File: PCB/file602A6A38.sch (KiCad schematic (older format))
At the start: 27 parts, among them IC4 74LV1T125GVH, IC5 74LV1T125GVH

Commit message: Completed parts details on schematics and recreated gerbers and bom.
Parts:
- IC4, IC5: LCSC (none) -> C75925
- R11, R12, R13, R14, R27, R28, R29, R31, R32, R33, R34, R35, R36, R37, R38, R39, R40, R41, R42, R43: LCSC (none) -> C17414; Manufacturer_Name (none) -> Vishay; Manufacturer_Part_Number (none) -> CRCW080510K0FKEAC; Mouser Part Number (none) -> 71-CRCW080510K0FKEAC
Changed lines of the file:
@@
 F 8 "Nexperia" H 3700 1700 50  0001 L CNN "Manufacturer_Name"
 F 9 "74LV1T125GVH" H 3700 1600 50  0001 L CNN "Manufacturer_Part_Number"
+F 10 "C75925" H 2850 2200 50  0001 C CNN "LCSC"
 	1    2850 2200
 	-1   0    0    1
@@
 F 8 "Nexperia" H 3700 2400 50  0001 L CNN "Manufacturer_Name"
 F 9 "74LV1T125GVH" H 3700 2300 50  0001 L CNN "Manufacturer_Part_Number"
+F 10 "C75925" H 2850 2900 50  0001 C CNN "LCSC"
 	1    2850 2900
 	-1   0    0    1
@@
 F 2 "Resistor_SMD:R_0805_2012Metric_Pad1.15x1.40mm_HandSolder" H 6600 2150 50  0001 C CNN
 F 3 "~" H 6600 2150 50  0001 C CNN
+F 4 "C17414" H 6600 2150 50  0001 C CNN "LCSC"
+F 5 "Vishay" H 6600 2150 50  0001 C CNN "Manufacturer_Name"
+F 6 "CRCW080510K0FKEAC" H 6600 2150 50  0001 C CNN "Manufacturer_Part_Number"
+F 7 "71-CRCW080510K0FKEAC" H 6600 2150 50  0001 C CNN "Mouser Part Number"
 	1    6600 2150
 	-1   0    0    1
@@
 F 2 "Resistor_SMD:R_0805_2012Metric_Pad1.15x1.40mm_HandSolder" H 6600 1250 50  0001 C CNN
 F 3 "~" H 6600 1250 50  0001 C CNN
+F 4 "C17414" H 6600 1250 50  0001 C CNN "LCSC"
+F 5 "Vishay" H 6600 1250 50  0001 C CNN "Manufacturer_Name"
+F 6 "CRCW080510K0FKEAC" H 6600 1250 50  0001 C CNN "Manufacturer_Part_Number"
+F 7 "71-CRCW080510K0FKEAC" H 6600 1250 50  0001 C CNN "Mouser Part Number"
 	1    6600 1250
 	1    0    0    -1
@@
 F 2 "Resistor_SMD:R_0805_2012Metric_Pad1.15x1.40mm_HandSolder" H 6500 1150 50  0001 C CNN
 F 3 "~" H 6500 1150 50  0001 C CNN
+F 4 "C17414" H 6500 1150 50  0001 C CNN "LCSC"
+F 5 "Vishay" H 6500 1150 50  0001 C CNN "Manufacturer_Name"
+F 6 "CRCW080510K0FKEAC" H 6500 1150 50  0001 C CNN "Manufacturer_Part_Number"
+F 7 "71-CRCW080510K0FKEAC" H 6500 1150 50  0001 C CNN "Mouser Part Number"
 	1    6500 1150
 	1    0    0    -1
@@
 F 2 "Resistor_SMD:R_0805_2012Metric_Pad1.15x1.40mm_HandSolder" H 6500 2050 50  0001 C CNN
 F 3 "~" H 6500 2050 50  0001 C CNN
+F 4 "C17414" H 6500 2050 50  0001 C CNN "LCSC"
+F 5 "Vishay" H 6500 2050 50  0001 C CNN "Manufacturer_Name"
+F 6 "CRCW080510K0FKEAC" H 6500 2050 50  0001 C CNN "Manufacturer_Part_Number"
+F 7 "71-CRCW080510K0FKEAC" H 6500 2050 50  0001 C CNN "Mouser Part Number"
 	1    6500 2050
 	-1   0    0    1
@@
 F 2 "Resistor_SMD:R_0805_2012Metric_Pad1.15x1.40mm_HandSolder" H 9050 2200 50  0001 C CNN
 F 3 "~" H 9050 2200 50  0001 C CNN
+F 4 "C17414" H 9050 2200 50  0001 C CNN "LCSC"
+F 5 "Vishay" H 9050 2200 50  0001 C CNN "Manufacturer_Name"
+F 6 "CRCW080510K0FKEAC" H 9050 2200 50  0001 C CNN "Manufacturer_Part_Number"
+F 7 "71-CRCW080510K0FKEAC" H 9050 2200 50  0001 C CNN "Mouser Part Number"
 	1    9050 2200
 	-1   0    0    1
@@
 F 2 "Resistor_SMD:R_0805_2012Metric_Pad1.15x1.40mm_HandSolder" H 9050 1300 50  0001 C CNN
 F 3 "~" H 9050 1300 50  0001 C CNN
+F 4 "C17414" H 9050 1300 50  0001 C CNN "LCSC"
+F 5 "Vishay" H 9050 1300 50  0001 C CNN "Manufacturer_Name"
+F 6 "CRCW080510K0FKEAC" H 9050 1300 50  0001 C CNN "Manufacturer_Part_Number"
+F 7 "71-CRCW080510K0FKEAC" H 9050 1300 50  0001 C CNN "Mouser Part Number"
 	1    9050 1300
 	1    0    0    -1
@@
 F 2 "Resistor_SMD:R_0805_2012Metric_Pad1.15x1.40mm_HandSolder" H 8950 1200 50  0001 C CNN
 F 3 "~" H 8950 1200 50  0001 C CNN
+F 4 "C17414" H 8950 1200 50  0001 C CNN "LCSC"
+F 5 "Vishay" H 8950 1200 50  0001 C CNN "Manufacturer_Name"
+F 6 "CRCW080510K0FKEAC" H 8950 1200 50  0001 C CNN "Manufacturer_Part_Number"
+F 7 "71-CRCW080510K0FKEAC" H 8950 1200 50  0001 C CNN "Mouser Part Number"
 	1    8950 1200
 	1    0    0    -1
@@
 F 2 "Resistor_SMD:R_0805_2012Metric_Pad1.15x1.40mm_HandSolder" H 8950 2100 50  0001 C CNN
 F 3 "~" H 8950 2100 50  0001 C CNN
+F 4 "C17414" H 8950 2100 50  0001 C CNN "LCSC"
+F 5 "Vishay" H 8950 2100 50  0001 C CNN "Manufacturer_Name"
+F 6 "CRCW080510K0FKEAC" H 8950 2100 50  0001 C CNN "Manufacturer_Part_Number"
+F 7 "71-CRCW080510K0FKEAC" H 8950 2100 50  0001 C CNN "Mouser Part Number"
 	1    8950 2100
 	-1   0    0    1
@@
 F 2 "Resistor_SMD:R_0805_2012Metric_Pad1.15x1.40mm_HandSolder" H 6550 4350 50  0001 C CNN
 F 3 "~" H 6550 4350 50  0001 C CNN
+F 4 "C17414" H 6550 4350 50  0001 C CNN "LCSC"
+F 5 "Vishay" H 6550 4350 50  0001 C CNN "Manufacturer_Name"
+F 6 "CRCW080510K0FKEAC" H 6550 4350 50  0001 C CNN "Manufacturer_Part_Number"
+F 7 "71-CRCW080510K0FKEAC" H 6550 4350 50  0001 C CNN "Mouser Part Number"
 	1    6550 4350
 	-1   0    0    1
@@
 F 2 "Resistor_SMD:R_0805_2012Metric_Pad1.15x1.40mm_HandSolder" H 6550 3450 50  0001 C CNN
 F 3 "~" H 6550 3450 50  0001 C CNN
+F 4 "C17414" H 6550 3450 50  0001 C CNN "LCSC"
+F 5 "Vishay" H 6550 3450 50  0001 C CNN "Manufacturer_Name"
+F 6 "CRCW080510K0FKEAC" H 6550 3450 50  0001 C CNN "Manufacturer_Part_Number"
+F 7 "71-CRCW080510K0FKEAC" H 6550 3450 50  0001 C CNN "Mouser Part Number"
 	1    6550 3450
 	1    0    0    -1
@@
 F 2 "Resistor_SMD:R_0805_2012Metric_Pad1.15x1.40mm_HandSolder" H 6450 3350 50  0001 C CNN
 F 3 "~" H 6450 3350 50  0001 C CNN
+F 4 "C17414" H 6450 3350 50  0001 C CNN "LCSC"
+F 5 "Vishay" H 6450 3350 50  0001 C CNN "Manufacturer_Name"
+F 6 "CRCW080510K0FKEAC" H 6450 3350 50  0001 C CNN "Manufacturer_Part_Number"
+F 7 "71-CRCW080510K0FKEAC" H 6450 3350 50  0001 C CNN "Mouser Part Number"
 	1    6450 3350
 	1    0    0    -1
@@
 F 2 "Resistor_SMD:R_0805_2012Metric_Pad1.15x1.40mm_HandSolder" H 6450 4250 50  0001 C CNN
 F 3 "~" H 6450 4250 50  0001 C CNN
+F 4 "C17414" H 6450 4250 50  0001 C CNN "LCSC"
+F 5 "Vishay" H 6450 4250 50  0001 C CNN "Manufacturer_Name"
+F 6 "CRCW080510K0FKEAC" H 6450 4250 50  0001 C CNN "Manufacturer_Part_Number"
+F 7 "71-CRCW080510K0FKEAC" H 6450 4250 50  0001 C CNN "Mouser Part Number"
 	1    6450 4250
 	-1   0    0    1
@@
 F 2 "Resistor_SMD:R_0805_2012Metric_Pad1.15x1.40mm_HandSolder" H 9050 4350 50  0001 C CNN
 F 3 "~" H 9050 4350 50  0001 C CNN
+F 4 "C17414" H 9050 4350 50  0001 C CNN "LCSC"
+F 5 "Vishay" H 9050 4350 50  0001 C CNN "Manufacturer_Name"
+F 6 "CRCW080510K0FKEAC" H 9050 4350 50  0001 C CNN "Manufacturer_Part_Number"
+F 7 "71-CRCW080510K0FKEAC" H 9050 4350 50  0001 C CNN "Mouser Part Number"
 	1    9050 4350
 	-1   0    0    1
@@
 F 2 "Resistor_SMD:R_0805_2012Metric_Pad1.15x1.40mm_HandSolder" H 9050 3450 50  0001 C CNN
 F 3 "~" H 9050 3450 50  0001 C CNN
+F 4 "C17414" H 9050 3450 50  0001 C CNN "LCSC"
+F 5 "Vishay" H 9050 3450 50  0001 C CNN "Manufacturer_Name"
+F 6 "CRCW080510K0FKEAC" H 9050 3450 50  0001 C CNN "Manufacturer_Part_Number"
+F 7 "71-CRCW080510K0FKEAC" H 9050 3450 50  0001 C CNN "Mouser Part Number"
 	1    9050 3450
 	1    0    0    -1
@@
 F 2 "Resistor_SMD:R_0805_2012Metric_Pad1.15x1.40mm_HandSolder" H 8950 3350 50  0001 C CNN
 F 3 "~" H 8950 3350 50  0001 C CNN
+F 4 "C17414" H 8950 3350 50  0001 C CNN "LCSC"
+F 5 "Vishay" H 8950 3350 50  0001 C CNN "Manufacturer_Name"
+F 6 "CRCW080510K0FKEAC" H 8950 3350 50  0001 C CNN "Manufacturer_Part_Number"
+F 7 "71-CRCW080510K0FKEAC" H 8950 3350 50  0001 C CNN "Mouser Part Number"
 	1    8950 3350
 	1    0    0    -1
@@
 F 2 "Resistor_SMD:R_0805_2012Metric_Pad1.15x1.40mm_HandSolder" H 8950 4250 50  0001 C CNN
 F 3 "~" H 8950 4250 50  0001 C CNN
+F 4 "C17414" H 8950 4250 50  0001 C CNN "LCSC"
+F 5 "Vishay" H 8950 4250 50  0001 C CNN "Manufacturer_Name"
+F 6 "CRCW080510K0FKEAC" H 8950 4250 50  0001 C CNN "Manufacturer_Part_Number"
+F 7 "71-CRCW080510K0FKEAC" H 8950 4250 50  0001 C CNN "Mouser Part Number"
 	1    8950 4250
 	-1   0    0    1
@@
 F 2 "Resistor_SMD:R_0805_2012Metric_Pad1.15x1.40mm_HandSolder" H 7750 1200 50  0001 C CNN
 F 3 "~" H 7750 1200 50  0001 C CNN
+F 4 "C17414" H 7750 1200 50  0001 C CNN "LCSC"
+F 5 "Vishay" H 7750 1200 50  0001 C CNN "Manufacturer_Name"
+F 6 "CRCW080510K0FKEAC" H 7750 1200 50  0001 C CNN "Manufacturer_Part_Number"
+F 7 "71-CRCW080510K0FKEAC" H 7750 1200 50  0001 C CNN "Mouser Part Number"
 	1    7750 1200
 	1    0    0    -1
@@
 F 2 "Resistor_SMD:R_0805_2012Metric_Pad1.15x1.40mm_HandSolder" H 10200 1200 50  0001 C CNN
 F 3 "~" H 10200 1200 50  0001 C CNN
+F 4 "C17414" H 10200 1200 50  0001 C CNN "LCSC"
+F 5 "Vishay" H 10200 1200 50  0001 C CNN "Manufacturer_Name"
+F 6 "CRCW080510K0FKEAC" H 10200 1200 50  0001 C CNN "Manufacturer_Part_Number"
+F 7 "71-CRCW080510K0FKEAC" H 10200 1200 50  0001 C CNN "Mouser Part Number"
 	1    10200 1200
 	1    0    0    -1
@@
 F 2 "Resistor_SMD:R_0805_2012Metric_Pad1.15x1.40mm_HandSolder" H 7700 3350 50  0001 C CNN
 F 3 "~" H 7700 3350 50  0001 C CNN
+F 4 "C17414" H 7700 3350 50  0001 C CNN "LCSC"
+F 5 "Vishay" H 7700 3350 50  0001 C CNN "Manufacturer_Name"
+F 6 "CRCW080510K0FKEAC" H 7700 3350 50  0001 C CNN "Manufacturer_Part_Number"
+F 7 "71-CRCW080510K0FKEAC" H 7700 3350 50  0001 C CNN "Mouser Part Number"
 	1    7700 3350
 	1    0    0    -1
@@
 F 2 "Resistor_SMD:R_0805_2012Metric_Pad1.15x1.40mm_HandSolder" H 10200 3350 50  0001 C CNN
 F 3 "~" H 10200 3350 50  0001 C CNN
+F 4 "C17414" H 10200 3350 50  0001 C CNN "LCSC"
+F 5 "Vishay" H 10200 3350 50  0001 C CNN "Manufacturer_Name"
+F 6 "CRCW080510K0FKEAC" H 10200 3350 50  0001 C CNN "Manufacturer_Part_Number"
+F 7 "71-CRCW080510K0FKEAC" H 10200 3350 50  0001 C CNN "Mouser Part Number"
 	1    10200 3350
 	1    0    0    -1

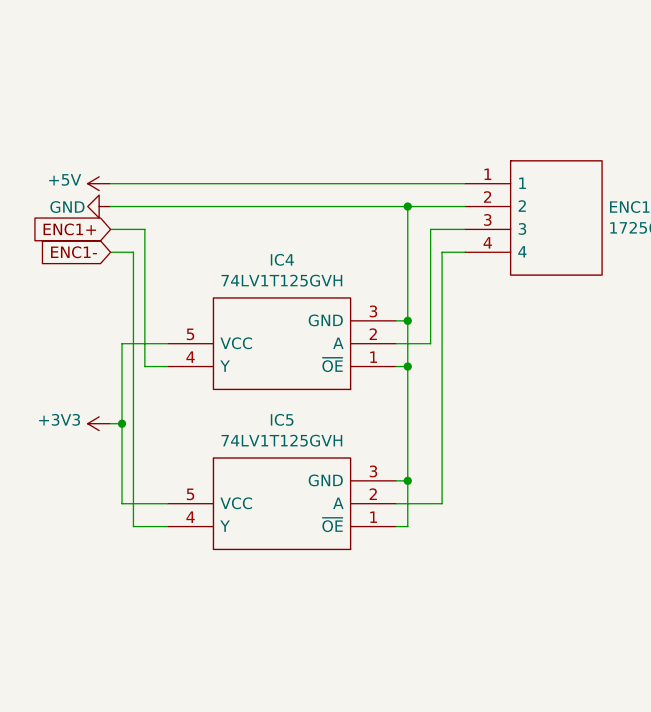
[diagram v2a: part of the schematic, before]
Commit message: Replaced RMS20 encoder with Chinese encoder. Maybe a modification of the encoder is necessary due to internal 7805 voltage regulator.
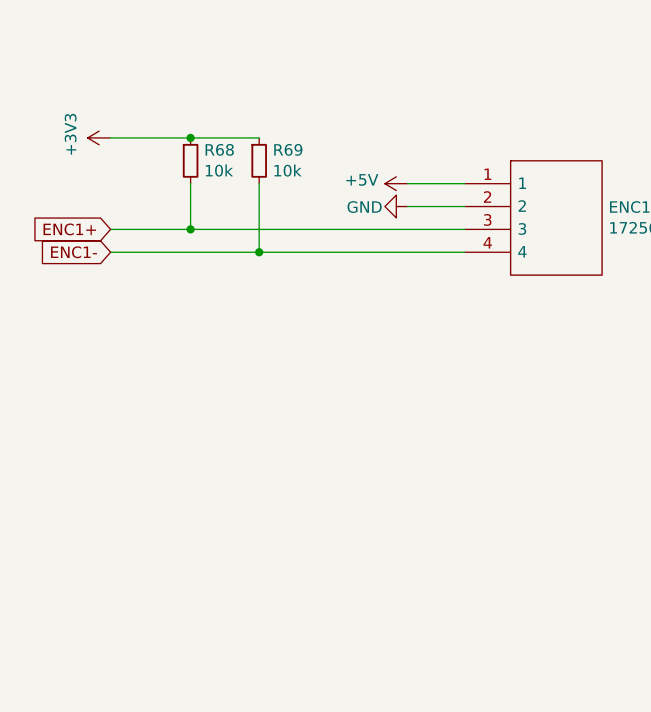
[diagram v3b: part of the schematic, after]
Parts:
- removed IC4, IC5: 74LV1T125GVH, SOT95P275X110-5N, symbol SamacSys_Parts:74LV1T125GVH
- added R68, R69: 10k, Resistor_SMD:R_0805_2012Metric_Pad1.15x1.40mm_HandSolder, symbol Device:R_Small
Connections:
- net +3V3: now also R68.1, R69.1
- net ENC1+: now also ENC1.3, R68.2
- net ENC1-: now also ENC1.4, R69.2
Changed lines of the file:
@@
 L power:GND #PWR?
 U 1 1 602AB8A6
-P 1600 1500
+P 2900 1500
 AR Path="/602AB8A6" Ref="#PWR?"  Part="1"
 AR Path="/602A6A39/602AB8A6" Ref="#PWR0133"  Part="1"
-F 0 "#PWR0133" H 1600 1250 50  0001 C CNN
-F 1 "GND" V 1604 1390 50  0000 R CNN
-F 2 "" H 1600 1500 50  0001 C CNN
-F 3 "" H 1600 1500 50  0001 C CNN
-	1    1600 1500
+F 0 "#PWR0133" H 2900 1250 50  0001 C CNN
+F 1 "GND" V 2904 1390 50  0000 R CNN
+F 2 "" H 2900 1500 50  0001 C CNN
+F 3 "" H 2900 1500 50  0001 C CNN
+	1    2900 1500
 	0    1    1    0
 $EndComp
@@
 	1    0    0    -1
 $EndComp
-$Comp
-L SamacSys_Parts:74LV1T125GVH IC4
-U 1 1 602B2EF5
-P 2850 2200
-F 0 "IC4" H 3350 1735 50  0000 C CNN
-F 1 "74LV1T125GVH" H 3350 1826 50  0000 C CNN
-F 2 "SOT95P275X110-5N" H 3700 2300 50  0001 L CNN
-F 3 "" H 3700 2200 50  0001 L CNN
-F 4 "Translation - Voltage Levels TRANSLATION - VOLTAGE LEVELS" H 3700 2100 50  0001 L CNN "Description"
-F 5 "1.1" H 3700 2000 50  0001 L CNN "Height"
-F 6 "771-74LV1T125GVH" H 3700 1900 50  0001 L CNN "Mouser Part Number"
-F 7 "https://www.mouser.co.uk/ProductDetail/Nexperia/74LV1T125GVH?qs=xZ%2FP%252Ba9zWqZTRKkicfFI6w%3D%3D" H 3700 1800 50  0001 L CNN "Mouser Price/Stock"
-F 8 "Nexperia" H 3700 1700 50  0001 L CNN "Manufacturer_Name"
-F 9 "74LV1T125GVH" H 3700 1600 50  0001 L CNN "Manufacturer_Part_Number"
-F 10 "C75925" H 2850 2200 50  0001 C CNN "LCSC"
-	1    2850 2200
-	-1   0    0    1
-$EndComp
-$Comp
-L SamacSys_Parts:74LV1T125GVH IC5
-U 1 1 602BE7C6
-P 2850 2900
-F 0 "IC5" H 3350 2435 50  0000 C CNN
-F 1 "74LV1T125GVH" H 3350 2526 50  0000 C CNN
-F 2 "SOT95P275X110-5N" H 3700 3000 50  0001 L CNN
-F 3 "" H 3700 2900 50  0001 L CNN
-F 4 "Translation - Voltage Levels TRANSLATION - VOLTAGE LEVELS" H 3700 2800 50  0001 L CNN "Description"
-F 5 "1.1" H 3700 2700 50  0001 L CNN "Height"
-F 6 "771-74LV1T125GVH" H 3700 2600 50  0001 L CNN "Mouser Part Number"
-F 7 "https://www.mouser.co.uk/ProductDetail/Nexperia/74LV1T125GVH?qs=xZ%2FP%252Ba9zWqZTRKkicfFI6w%3D%3D" H 3700 2500 50  0001 L CNN "Mouser Price/Stock"
-F 8 "Nexperia" H 3700 2400 50  0001 L CNN "Manufacturer_Name"
-F 9 "74LV1T125GVH" H 3700 2300 50  0001 L CNN "Manufacturer_Part_Number"
-F 10 "C75925" H 2850 2900 50  0001 C CNN "LCSC"
-	1    2850 2900
-	-1   0    0    1
-$EndComp
-Wire Wire Line
-	2900 1500 2900 2000
-Wire Wire Line
-	2900 2000 2850 2000
-Connection ~ 2900 1500
-Wire Wire Line
-	2900 1500 3150 1500
-Wire Wire Line
-	2900 2000 2900 2200
-Wire Wire Line
-	2900 2200 2850 2200
-Connection ~ 2900 2000
-Wire Wire Line
-	2900 2200 2900 2700
-Wire Wire Line
-	2900 2700 2850 2700
-Connection ~ 2900 2200
-Wire Wire Line
-	2900 2700 2900 2900
-Wire Wire Line
-	2900 2900 2850 2900
-Connection ~ 2900 2700
-Wire Wire Line
-	2850 2100 3000 2100
-Wire Wire Line
-	3000 2100 3000 1600
-Wire Wire Line
-	3000 1600 3150 1600
-Wire Wire Line
-	3150 1700 3050 1700
-Wire Wire Line
-	3050 1700 3050 2800
-Wire Wire Line
-	3050 2800 2850 2800
-Wire Wire Line
-	1700 1700 1700 2900
-Wire Wire Line
-	1700 2900 1850 2900
-Wire Wire Line
-	1850 2200 1750 2200
-Wire Wire Line
-	1750 2200 1750 1600
-Wire Wire Line
-	1600 1400 3150 1400
-Wire Wire Line
-	1600 1500 2900 1500
-Wire Wire Line
-	1600 1600 1750 1600
-Wire Wire Line
-	1700 1700 1600 1700
-Wire Wire Line
-	1850 2800 1650 2800
-Wire Wire Line
-	1650 2800 1650 2450
-Wire Wire Line
-	1650 2450 1600 2450
-Wire Wire Line
-	1650 2450 1650 2100
-Wire Wire Line
-	1650 2100 1850 2100
-Connection ~ 1650 2450
 Text GLabel 6400 1500 0    50   Input ~ 0
 ENC2_A1
@@
 L power:+5V #PWR0134
 U 1 1 60545589
-P 1600 1400
-F 0 "#PWR0134" H 1600 1250 50  0001 C CNN
-F 1 "+5V" V 1615 1528 50  0000 L CNN
-F 2 "" H 1600 1400 50  0001 C CNN
-F 3 "" H 1600 1400 50  0001 C CNN
-	1    1600 1400
+P 2900 1400
+F 0 "#PWR0134" H 2900 1250 50  0001 C CNN
+F 1 "+5V" V 2915 1528 50  0000 L CNN
+F 2 "" H 2900 1400 50  0001 C CNN
+F 3 "" H 2900 1400 50  0001 C CNN
+	1    2900 1400
 	0    -1   -1   0
 $EndComp
@@
 	10450 3800 10200 3800
 Connection ~ 10200 3800
-$Comp
-L power:+3V3 #PWR0156
-U 1 1 603A7D0F
-P 1600 2450
-F 0 "#PWR0156" H 1600 2300 50  0001 C CNN
-F 1 "+3V3" V 1615 2578 50  0000 L CNN
-F 2 "" H 1600 2450 50  0001 C CNN
-F 3 "" H 1600 2450 50  0001 C CNN
-	1    1600 2450
-	0    -1   -1   0
-$EndComp
 Wire Wire Line
 	8950 950  9050 950
@@
 Wire Wire Line
 	7100 900  7750 900
+$Comp
+L Device:R_Small R68
+U 1 1 6034B98A
+P 1950 1300
+F 0 "R68" H 2009 1346 50  0000 L CNN
+F 1 "10k" H 2009 1255 50  0000 L CNN
+F 2 "Resistor_SMD:R_0805_2012Metric_Pad1.15x1.40mm_HandSolder" H 1950 1300 50  0001 C CNN
+F 3 "~" H 1950 1300 50  0001 C CNN
+F 4 "C17414" H 1950 1300 50  0001 C CNN "LCSC"
+F 5 "Vishay" H 1950 1300 50  0001 C CNN "Manufacturer_Name"
+F 6 "CRCW080510K0FKEAC" H 1950 1300 50  0001 C CNN "Manufacturer_Part_Number"
+F 7 "71-CRCW080510K0FKEAC" H 1950 1300 50  0001 C CNN "Mouser Part Number"
+	1    1950 1300
+	1    0    0    -1
+$EndComp
+$Comp
+L Device:R_Small R69
+U 1 1 6034BF11
+P 2250 1300
+F 0 "R69" H 2309 1346 50  0000 L CNN
+F 1 "10k" H 2309 1255 50  0000 L CNN
+F 2 "Resistor_SMD:R_0805_2012Metric_Pad1.15x1.40mm_HandSolder" H 2250 1300 50  0001 C CNN
+F 3 "~" H 2250 1300 50  0001 C CNN
+F 4 "C17414" H 2250 1300 50  0001 C CNN "LCSC"
+F 5 "Vishay" H 2250 1300 50  0001 C CNN "Manufacturer_Name"
+F 6 "CRCW080510K0FKEAC" H 2250 1300 50  0001 C CNN "Manufacturer_Part_Number"
+F 7 "71-CRCW080510K0FKEAC" H 2250 1300 50  0001 C CNN "Mouser Part Number"
+	1    2250 1300
+	1    0    0    -1
+$EndComp
+Wire Wire Line
+	2900 1500 3150 1500
+Wire Wire Line
+	1600 1200 1950 1200
+Connection ~ 1950 1200
+Wire Wire Line
+	1950 1200 2250 1200
+Wire Wire Line
+	1600 1600 1950 1600
+Wire Wire Line
+	1600 1700 2250 1700
+Wire Wire Line
+	1950 1400 1950 1600
+Connection ~ 1950 1600
+Wire Wire Line
+	1950 1600 3150 1600
+Wire Wire Line
+	2250 1400 2250 1700
+Connection ~ 2250 1700
+Wire Wire Line
+	2250 1700 3150 1700
+$Comp
+L power:+3V3 #PWR0122
+U 1 1 6037248A
+P 1600 1200
+F 0 "#PWR0122" H 1600 1050 50  0001 C CNN
+F 1 "+3V3" H 1615 1373 50  0000 C CNN
+F 2 "" H 1600 1200 50  0001 C CNN
+F 3 "" H 1600 1200 50  0001 C CNN
+	1    1600 1200
+	0    -1   -1   0
+$EndComp
+Wire Wire Line
+	2900 1400 3150 1400
 $EndSCHEMATC
